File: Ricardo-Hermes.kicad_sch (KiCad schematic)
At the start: 43 parts, among them J1 RBUS, U1 ESP32-S3, Y1 R940000171

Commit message: Finishing touches without BOM
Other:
- moved on the sheet: H1, H2, H3, H4, J1, POWER_UART1

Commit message: finishing changes
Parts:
- added R7: 499R, Resistor_SMD:R_0402_1005Metric, symbol Device:R_Small
- added UART_ESP1: Conn_01x03, Connector_PinHeader_2.54mm:PinHeader_1x03_P2.54mm_Vertical, symbol Connector_Generic:Conn_01x03
- 3V3LED1, CRXLED1, CTXLED1, TXLED1: footprint Resistor_SMD:R_0402_1005Metric -> Diode_SMD:D_0402_1005Metric
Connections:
- net GND: now also UART_ESP1.1 (Pin_1)
- net RXD: now also U1.48 (MTMS/JTAG/GPIO42); no longer U1.50 (U0RXD/PROG/GPIO44)
- net TXD: now also R7.1; no longer R6.1
- net at U1.47 (MTDI/JTAG/GPIO41): now also R7.2
- new net RXD_ESP: U1.50 (U0RXD/PROG/GPIO44), UART_ESP1.2 (Pin_2)
- new net TXD_ESP: R6.1, UART_ESP1.3 (Pin_3)
- no-connect marks 4 -> 23

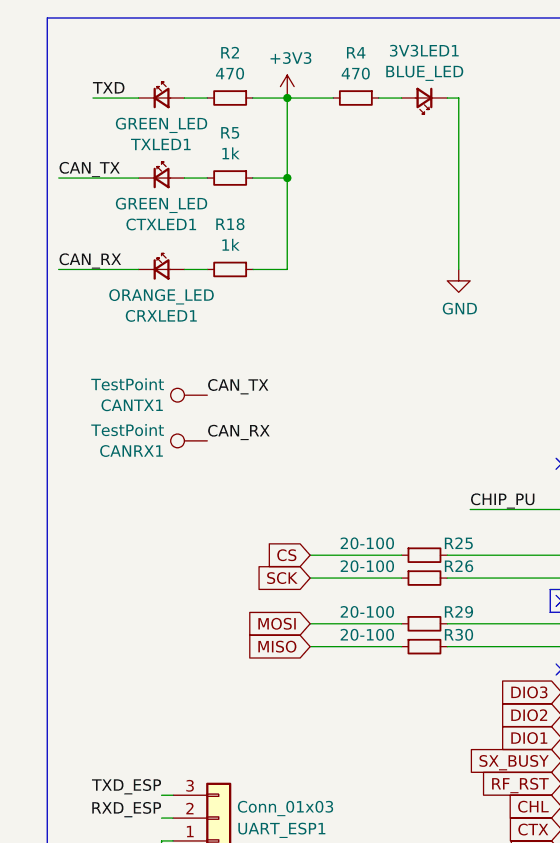
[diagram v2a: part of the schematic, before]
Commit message: New leds
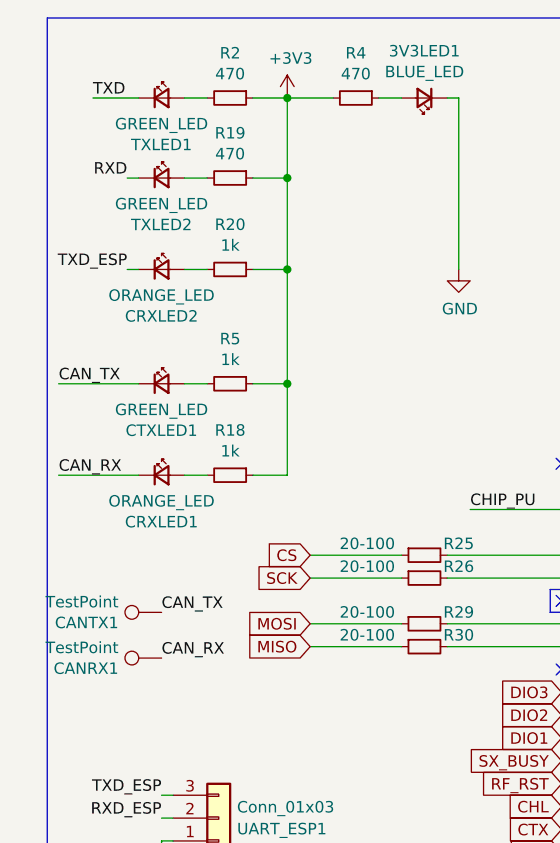
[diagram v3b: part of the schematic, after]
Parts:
- added CRXLED2: ORANGE_LED, Diode_SMD:D_0402_1005Metric, symbol Device:LED_Small
- added R19: 470, Resistor_SMD:R_0402_1005Metric, symbol Device:R_Small
- added R20: 1k, Resistor_SMD:R_0402_1005Metric, symbol Device:R_Small
- added TXLED2: GREEN_LED, Diode_SMD:D_0402_1005Metric, symbol Device:LED_Small
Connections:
- net +3V3: now also R19.1, R20.1
- net RXD: now also TXLED2.1 (K)
- net TXD_ESP: now also CRXLED2.1 (K)
- new net: CRXLED2.2 (A), R20.2
- new net: R19.2, TXLED2.2 (A)
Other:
- moved on the sheet: CANRX1, CANTX1, CRXLED1, CTXLED1, R18, R5

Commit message: Final fixes
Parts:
- ESP_TX_LED1: renamed from CRXLED2; value ORANGE_LED -> GREEN_LED
- RXLED2: renamed from TXLED2; value GREEN_LED -> ORANGE_LED
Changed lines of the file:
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@@
 		(on_board yes)
 		(dnp no)
-		(property "Reference" "CRXLED2"
+		(property "Reference" "ESP_TX_LED1"
 			(at 25.4 45.847 0)
 			(effects
@@
 			)
 		)
-		(property "Value" "ORANGE_LED"
+		(property "Value" "GREEN_LED"
 			(at 25.4 43.5356 0)
 			(effects
@@
 			(project "Ricardo-Hermes"
 				(path "/7db990e4-92e1-4f99-b4d2-435bbec1ba83"
-					(reference "CRXLED2")
+					(reference "ESP_TX_LED1")
 					(unit 1)
 				)
@@
 		(on_board yes)
 		(dnp no)
-		(property "Reference" "TXLED2"
+		(property "Reference" "RXLED2"
 			(at 25.4 35.687 0)
 			(effects
@@
 			)
 		)
-		(property "Value" "GREEN_LED"
+		(property "Value" "ORANGE_LED"
 			(at 25.4 33.3756 0)
 			(effects
@@
 			(project "Ricardo-Hermes"
 				(path "/7db990e4-92e1-4f99-b4d2-435bbec1ba83"
-					(reference "TXLED2")
-					(unit 1)
-				)
+					(reference "RXLED2")
+					(unit 1)
+				)
